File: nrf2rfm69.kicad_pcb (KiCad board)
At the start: 2 copper layers, 17.5 x 30 mm, 4 parts, among them P1 CONN_01X01, U1 RFM69HW, U2 NRF24L01

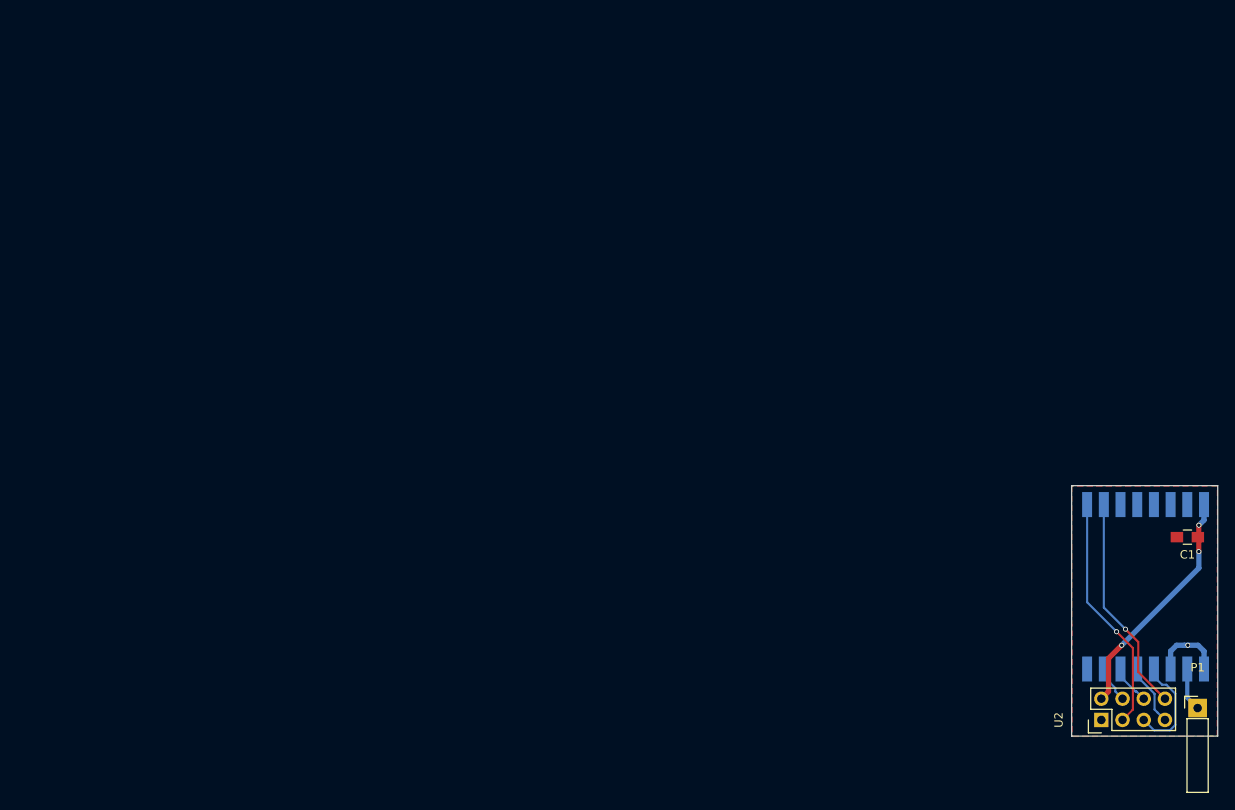
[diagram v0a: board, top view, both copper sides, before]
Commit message: Shrinked pcb a bit, and created panel layout for dirtypcb's
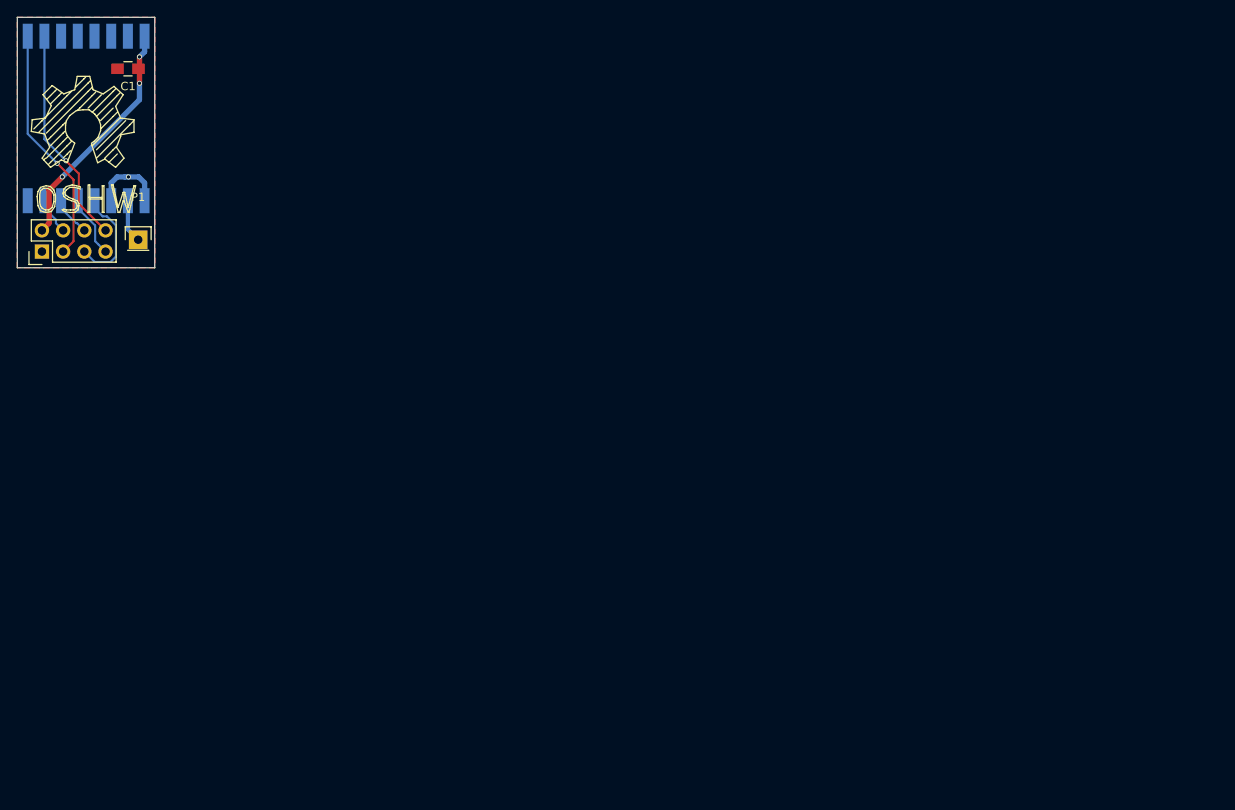
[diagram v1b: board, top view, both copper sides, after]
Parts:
- added REF**: Symbol_OSHW-Logo_SilkScreen_BIG, Symbols:Symbol_OSHW-Logo_SilkScreen_BIG, F.Cu at (24.7, 8.77)
- P1: footprint Socket_Strips:Socket_Strip_Angled_1x01 -> Pin_Headers:Pin_Header_Straight_1x01
- moved U1 138.7 mm to (18.0, 18.6)
- moved C1 138.7 mm to (30.0, 21.1)
- moved P1 138.7 mm to (31.2, 41.5)
- moved U2 138.7 mm to (19.7, 43.0)
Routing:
- net (no net): track 107.6 -> 107.0 mm
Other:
- board size 17.5 x 30 mm -> 16.5 x 30 mm
